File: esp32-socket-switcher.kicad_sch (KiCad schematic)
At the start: 27 parts, among them J1 USB4110GFA, J2 4DB-P108-06, K1 G5CA-1A DC5, Q3 CSD17575Q3T, SW1 SW_SPST

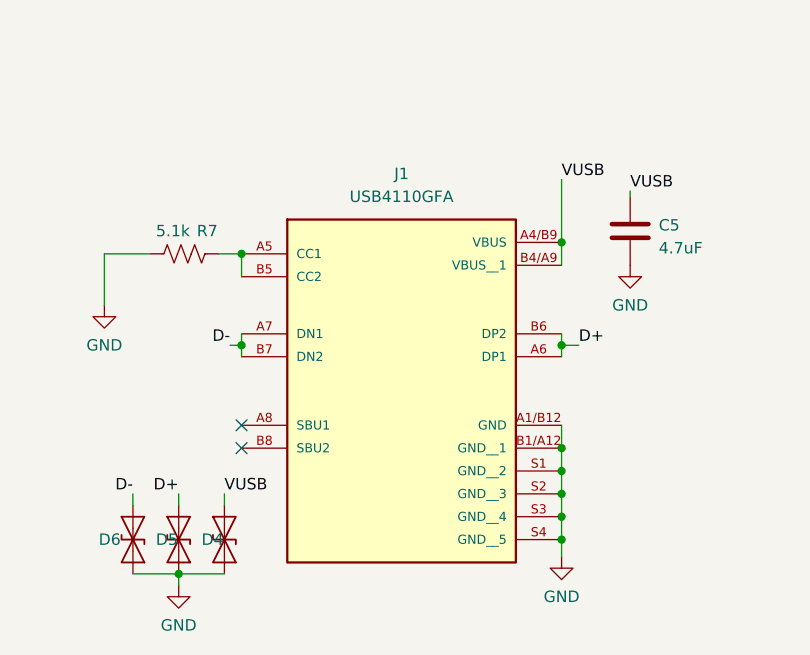
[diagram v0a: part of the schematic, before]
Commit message: updated usbc connector to one that's ACTUALLY FUCKING IN STOCK
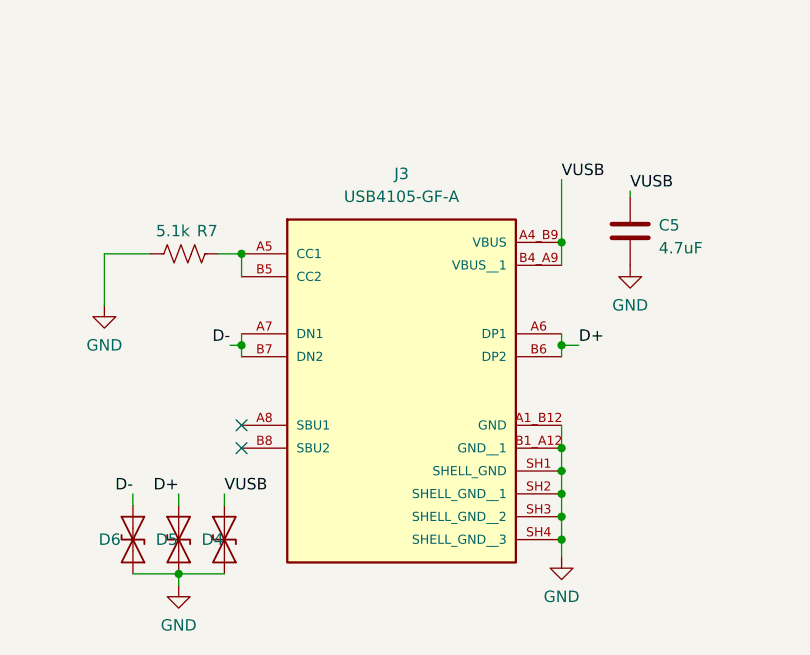
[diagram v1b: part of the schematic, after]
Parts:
- removed J1: USB4110GFA, esp32-socket-switcher:GCT_USB4110GFA, symbol esp32-socket-switcher:USB4110GFA
- added J3: USB4105-GF-A, esp32-socket-switcher:GCT_USB4105-GF-A, symbol esp32-socket-switcher:USB4105-GF-A
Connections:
- net D+: now also J3.A6 (DP1), J3.B6 (DP2)
- net D-: now also J3.A7 (DN1), J3.B7 (DN2)
- net GND: now also J3.A1_B12 (GND), J3.B1_A12 (GND__1), J3.SH1 (SHELL_GND), J3.SH2 (SHELL_GND__1), J3.SH3 (SHELL_GND__2), J3.SH4 (SHELL_GND__3)
- net VUSB: now also J3.A4_B9 (VBUS), J3.B4_A9 (VBUS__1)
- net at R7.2: now also J3.A5 (CC1), J3.B5 (CC2)
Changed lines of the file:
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@@
+    (stroke (width 0) (type default))
+  )
+  (wire (pts (xy 64.77 24.13) (xy 63.5 24.13))
+    (stroke (width 0) (type default))
+  )
+  (wire (pts (xy 242.57 92.71) (xy 246.38 92.71))
+    (stroke (width 0) (type default))
+  )
+  (wire (pts (xy 92.71 44.45) (xy 95.25 44.45))
     (stroke (width 0) (type default))
   )
   (wire (pts (xy 71.12 146.685) (xy 71.12 153.67))
-    (stroke (width 0) (type default))
-  )
-  (wire (pts (xy 64.77 24.13) (xy 63.5 24.13))
-    (stroke (width 0) (type default))
-  )
-  (wire (pts (xy 242.57 92.71) (xy 246.38 92.71))
-    (stroke (width 0) (type default))
-  )
-  (wire (pts (xy 92.71 44.45) (xy 95.25 44.45))
     (stroke (width 0) (type default))
   )
@@
     )
   )
+  (symbol (lib_id "esp32-socket-switcher:USB4105-GF-A") (at 53.34 163.83 0) (unit 1)
+    (in_bom yes) (on_board yes) (dnp no) (fields_autoplaced)
+    (property "Reference" "J3" (at 53.34 146.05 0)
+      (effects (font (size 1.27 1.27)))
+    )
+    (property "Value" "USB4105-GF-A" (at 53.34 148.59 0)
+      (effects (font (size 1.27 1.27)))
+    )
+    (property "Footprint" "esp32-socket-switcher:GCT_USB4105-GF-A" (at 53.34 163.83 0)
+      (effects (font (size 1.27 1.27)) (justify bottom) hide)
+    )
+    (property "Datasheet" "" (at 53.34 163.83 0)
+      (effects (font (size 1.27 1.27)) hide)
+    )
+    (property "PARTREV" "B3" (at 53.34 163.83 0)
+      (effects (font (size 1.27 1.27)) (justify bottom) hide)
+    )
+    (property "MANUFACTURER" "Global Connector Technology" (at 53.34 163.83 0)
+      (effects (font (size 1.27 1.27)) (justify bottom) hide)
+    )
+    (property "MAXIMUM_PACKAGE_HEIGHT" "3.31mm" (at 53.34 163.83 0)
+      (effects (font (size 1.27 1.27)) (justify bottom) hide)
+    )
+    (property "STANDARD" "Manufacturer Recommendations" (at 53.34 163.83 0)
+      (effects (font (size 1.27 1.27)) (justify bottom) hide)
+    )
+    (pin "A1_B12")
+    (pin "A4_B9")
+    (pin "A5")
+    (pin "A6")
+    (pin "A7")
+    (pin "A8")
+    (pin "B1_A12")
+    (pin "B4_A9")
+    (pin "B5")
+    (pin "B6")
+    (pin "B7")
+    (pin "B8")
+    (pin "SH1")
+    (pin "SH2")
+    (pin "SH3")
+    (pin "SH4")
+    (instances
+      (project "esp32-socket-switcher"
+        (path "/19e4cb9f-d0a4-4ce0-8aa4-5fe95563dc37"
+          (reference "J3") (unit 1)
+        )
+      )
+    )
+  )
   (symbol (lib_id "esp32-socket-switcher:ESD9B3.3ST5G") (at 23.495 186.69 90) (unit 1)
     (in_bom yes) (on_board yes) (dnp no)
@@
         )
       )
-    )
-  )
-  (symbol (lib_id "esp32-socket-switcher:USB4110GFA") (at 53.34 161.29 0) (unit 1)
-    (in_bom yes) (on_board yes) (dnp no) (fields_autoplaced)
-    (property "Reference" "J1" (at 53.34 146.05 0)
-      (effects (font (size 1.27 1.27)))
-    )
-    (property "Value" "USB4110GFA" (at 53.34 148.59 0)
-      (effects (font (size 1.27 1.27)))
-    )
-    (property "Footprint" "esp32-socket-switcher:GCT_USB4110GFA" (at 53.34 161.29 0)
-      (effects (font (size 1.27 1.27)) (justify bottom) hide)
-    )
-    (property "Datasheet" "" (at 53.34 161.29 0)
-      (effects (font (size 1.27 1.27)) hide)
-    )
-    (property "MF" "GCT" (at 53.34 161.29 0)
-      (effects (font (size 1.27 1.27)) (justify bottom) hide)
-    )
-    (property "Description" "USB-C (USB TYPE-C) USB 2.0 Receptacle Connector 24 (16+8 Dummy) Position Surface Mount, Right Angle; Through Hole" (at 53.34 161.29 0)
-      (effects (font (size 1.27 1.27)) (justify bottom) hide)
-    )
-    (property "Package" "None" (at 53.34 161.29 0)
-      (effects (font (size 1.27 1.27)) (justify bottom) hide)
-    )
-    (property "Price" "None" (at 53.34 161.29 0)
-      (effects (font (size 1.27 1.27)) (justify bottom) hide)
-    )
-    (property "MP" "USB4110GFA" (at 53.34 161.29 0)
-      (effects (font (size 1.27 1.27)) (justify bottom) hide)
-    )
-    (property "Availability" "In Stock" (at 53.34 161.29 0)
-      (effects (font (size 1.27 1.27)) (justify bottom) hide)
-    )
-    (pin "A1/B12")
-    (pin "A4/B9")
-    (pin "A5")
-    (pin "A6")
-    (pin "A7")
-    (pin "A8")
-    (pin "B1/A12")
-    (pin "B4/A9")
-    (pin "B5")
-    (pin "B6")
-    (pin "B7")
-    (pin "B8")
-    (pin "S1")
-    (pin "S2")
-    (pin "S3")
-    (pin "S4")
-    (instances
-      (project "esp32-socket-switcher"
-        (path "/19e4cb9f-d0a4-4ce0-8aa4-5fe95563dc37"
-          (reference "J1") (unit 1)
-        )
-      )
